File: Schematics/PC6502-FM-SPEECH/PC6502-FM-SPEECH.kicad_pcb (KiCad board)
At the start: 4 copper layers, 100 x 100 mm, 77 parts, among them J1 BUS, J2 SJ-3523-SMT-TR, J5 Conn_02x05_Odd_Even, U1 ATF1502AS, U2 MCP6002-xSN, U3 MCP6002-xSN, U4 YMF262-M, U5 SP0256-AL2, U6 MCP6002-xSN, U7 YAC512-M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

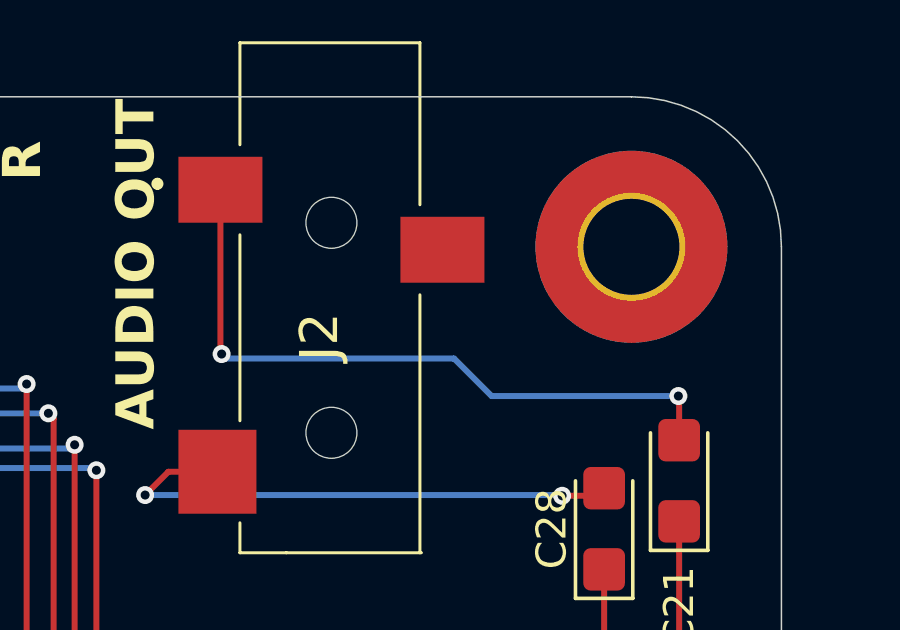
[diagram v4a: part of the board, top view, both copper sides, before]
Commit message: Fixed output on FM/Speech card
The ring and sleeve were the wrong way around.
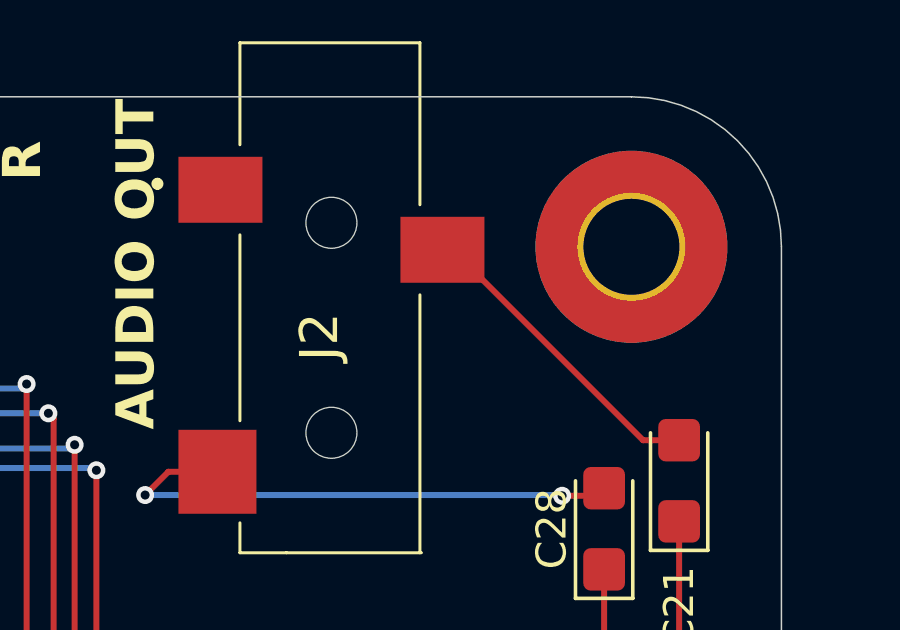
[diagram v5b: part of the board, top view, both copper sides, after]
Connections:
- C21 pad 2: Net-(J2-SLEEVE) -> Net-(J2-RING)
- J2 pad 1: Net-(J2-SLEEVE) -> GND
- J2 pad 3: GND -> Net-(J2-RING)
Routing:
- net Net-(J2-SLEEVE): track 22.8 -> 0.00 mm, vias 2 -> 0
- net Net-(J2-RING): track 0.00 -> 10.5 mm
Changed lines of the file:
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@@
 	(net 108 "unconnected-(U4-TEST-Pad9)")
 	(net 109 "/OPL/DOCD")
-	(net 110 "Net-(J2-SLEEVE)")
+	(net 110 "Net-(J2-RING)")
 	(net 111 "Net-(J2-TIP)")
 	(footprint "MountingHole:MountingHole_3.2mm_M3_Pad_TopBottom"
@@
 			(layers "F.Cu" "F.Mask" "F.Paste")
 			(roundrect_rratio 0.179856)
-			(net 110 "Net-(J2-SLEEVE)")
+			(net 110 "Net-(J2-RING)")
 			(pintype "passive")
 		)
@@
 			(size 2.2 2.8)
 			(layers "F.Cu" "F.Mask" "F.Paste")
-			(net 110 "Net-(J2-SLEEVE)")
+			(net 1 "GND")
 			(pinfunction "SLEEVE")
 			(pintype "passive")
@@
 			(size 2.2 2.8)
 			(layers "F.Cu" "F.Mask" "F.Paste")
-			(net 1 "GND")
+			(net 110 "Net-(J2-RING)")
 			(pinfunction "RING")
 			(pintype "passive")
@@
 	)
 	(segment
-		(start 178.36 53.535)
-		(end 178.36 48.1)
-		(width 0.2)
-		(layer "F.Cu")
-		(net 110)
-	)
-	(segment
-		(start 178.4 53.575)
-		(end 178.36 53.535)
-		(width 0.2)
-		(layer "F.Cu")
-		(net 110)
-	)
-	(segment
-		(start 193.65 55)
-		(end 193.625 54.975)
+		(start 186.1 50.1)
+		(end 185.76 50.1)
 		(width 0.2)
 		(layer "F.Cu")
@@
 	(segment
 		(start 193.65 56.4475)
-		(end 193.65 55)
+		(end 192.4475 56.4475)
 		(width 0.2)
 		(layer "F.Cu")
 		(net 110)
 	)
-	(via
-		(at 178.4 53.575)
-		(size 0.6)
-		(drill 0.3)
-		(layers "F.Cu" "B.Cu")
-		(net 110)
-	)
-	(via
-		(at 193.625 54.975)
-		(size 0.6)
-		(drill 0.3)
-		(layers "F.Cu" "B.Cu")
-		(net 110)
-	)
-	(segment
-		(start 187.4 54.975)
-		(end 186.15 53.725)
-		(width 0.2)
-		(layer "B.Cu")
-		(net 110)
-	)
-	(segment
-		(start 186.15 53.725)
-		(end 178.55 53.725)
-		(width 0.2)
-		(layer "B.Cu")
-		(net 110)
-	)
-	(segment
-		(start 178.55 53.725)
-		(end 178.4 53.575)
-		(width 0.2)
-		(layer "B.Cu")
-		(net 110)
-	)
 	(segment
-		(start 193.625 54.975)
-		(end 187.4 54.975)
+		(start 192.4475 56.4475)
+		(end 186.1 50.1)
 		(width 0.2)
-		(layer "B.Cu")
+		(layer "F.Cu")
 		(net 110)
 	)
